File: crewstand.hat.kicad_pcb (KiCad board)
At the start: 2 copper layers, 113 x 70.5 mm, 21 parts, among them J2 CAN Terminal, J3 Sensor Terminal, J4 V-In, J5 Relais Out, J6 V-Out, Y1 12M

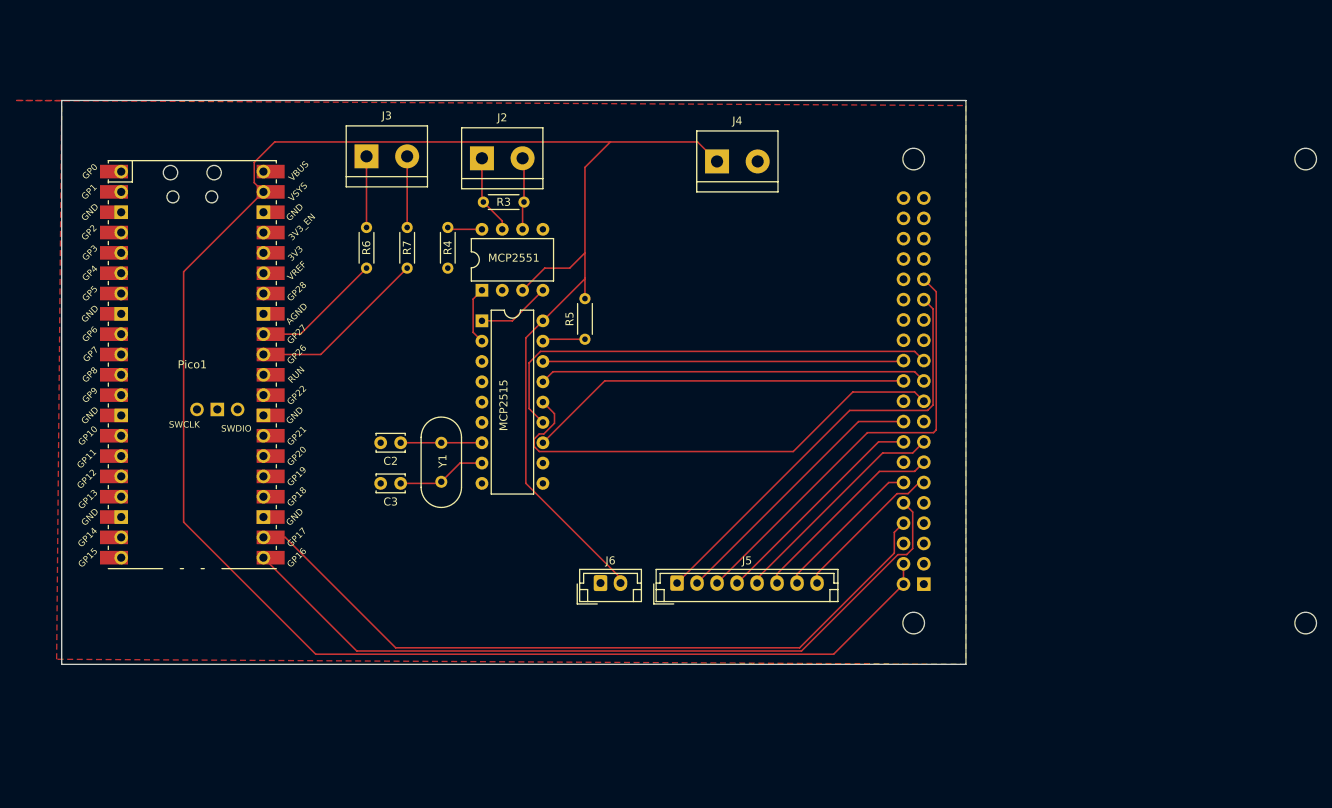
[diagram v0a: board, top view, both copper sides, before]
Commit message: feat: use jst connectors
* update clearance and track width
* Optimize placement and tracks

issue #2
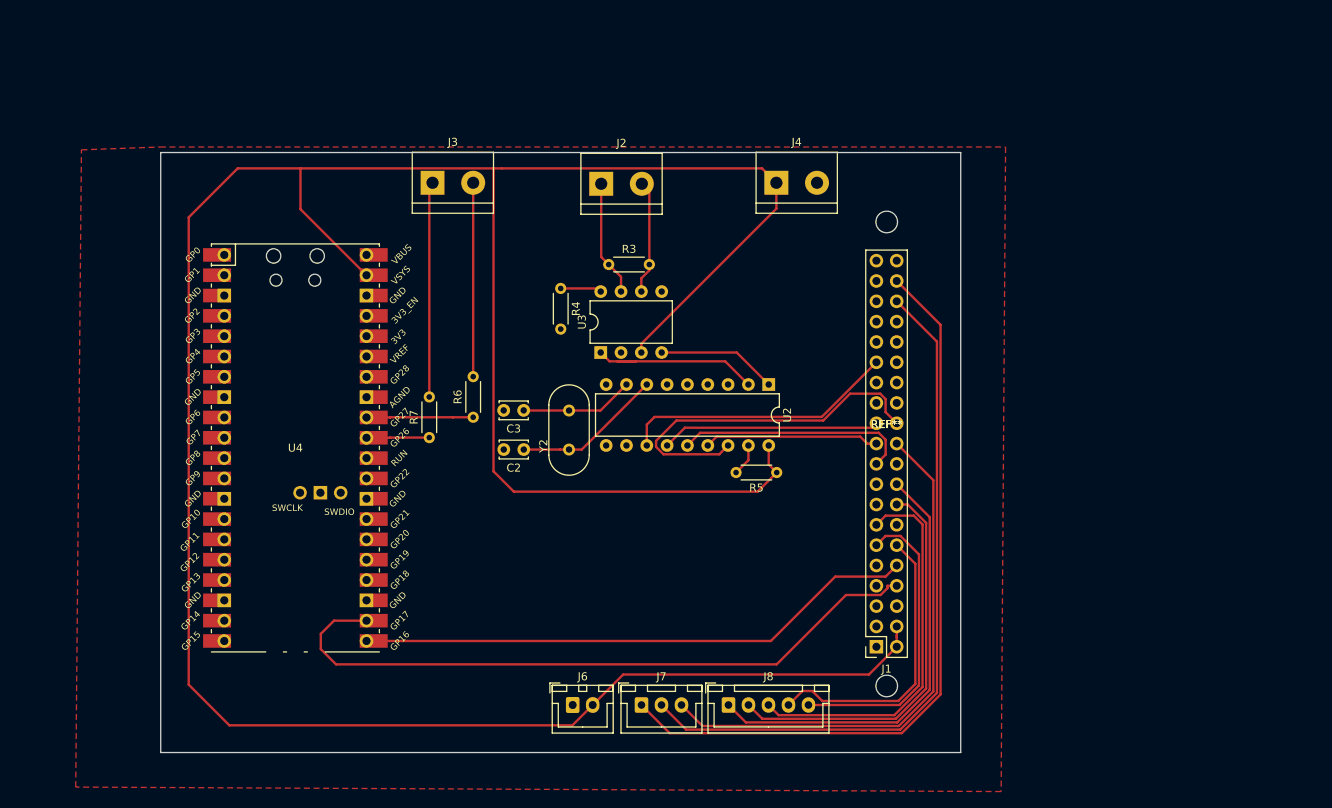
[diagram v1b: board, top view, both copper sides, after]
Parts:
- removed J5: Relais Out, Connector_JST:JST_EH_B8B-EH-A_1x08_P2.50mm_Vertical
- removed MCP2515: MCP2515-xSO, Package_DIP:DIP-18_W7.62mm
- removed MCP2551: MCP2551-I-P, Package_DIP:DIP-8_W7.62mm
- removed MH1, MH2, MH3, MH4: MountingHole_2.7mm_M2.5, MountingHole:MountingHole_2.7mm_M2.5
- removed Pico1: PicoW, RaspberryPi:RPi_PicoW_SMD_TH
- removed RPi1: GPIO, Connector_PinSocket_2.54mm:PinSocket_2x20_P2.54mm_Vertical
- removed Y1: 12M, Crystal:Crystal_HC49-U_Vertical
- added J1: GPIO, Connector_PinSocket_2.54mm:PinSocket_2x20_P2.54mm_Vertical, F.Cu at (249.5, 191.8)
- added J7: Relais2, Connector_JST:JST_XH_B3B-XH-A_1x03_P2.50mm_Vertical, F.Cu at (220.1, 199.1)
- added J8: Relais1, Connector_JST:JST_XH_B5B-XH-A_1x05_P2.50mm_Vertical, F.Cu at (231.0, 199.1)
- added REF** (x2): MountingHole_2.7mm_M2.5, MountingHole:MountingHole_2.7mm_M2.5, F.Cu at (250.8, 167.7)
- added U2: MCP2515-xSO, Package_DIP:DIP-18_W7.62mm, F.Cu at (236.0, 159.0)
- added U3: MCP2551-I-P, Package_DIP:DIP-8_W7.62mm, F.Cu at (215.0, 155.0)
- added U4: PicoW, RaspberryPI PicoW:RPi_PicoW_SMD_TH, F.Cu at (176.8, 166.9)
- added Y2: 12M, Crystal:Crystal_HC49-U_Vertical, F.Cu at (211.0, 167.1)
- J6: footprint Connector_JST:JST_EH_B2B-EH-A_1x02_P2.50mm_Vertical -> Connector_JST:JST_XH_B2B-XH-A_1x02_P2.50mm_Vertical
- moved R5 32.4 mm to (237.0, 170.0), turned to 180 degrees
- moved R6 22.9 mm to (199.1, 163.1)
- moved R7 21.4 mm to (193.6, 165.6)
- moved C3 17.9 mm to (205.4, 162.2)
- moved R3 17.5 mm to (216.0, 144.0)
- moved R4 16.0 mm to (210.0, 147.0)
- moved J6 15.6 mm to (211.5, 199.1)
- moved C2 15.4 mm to (205.4, 167.1)
- moved J2 15.2 mm to (215.1, 133.9)
- moved J3 8.89 mm to (194.0, 133.8)
- moved J4 7.88 mm to (237.0, 133.8)
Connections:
- R6 pad 2: Net-(J3-Pin_1) -> Net-(J3-Pin_2)
- R7 pad 2: Net-(J3-Pin_2) -> Net-(J3-Pin_1)
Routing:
- net /GPIO20/PCM.DIN: track 0.00 -> 94.8 mm
- net /GPIO16: track 0.00 -> 88.6 mm
- net +5V: track 289.5 -> 356.5 mm
- net /GPIO6: track 54.8 -> 0.00 mm
- net /GPIO11/SPI0.SCLK: track 58.6 -> 27.3 mm
- net /GPIO10/SPI0.MOSI: track 60.1 -> 29.3 mm
- net /GPIO22: track 28.5 -> 0.00 mm
- net /GPIO15/RXD0: track 97.5 -> 70.2 mm
- net /GPIO9/SPI0.MISO: track 48.6 -> 21.9 mm
- net /GPIO27: track 25.3 -> 48.3 mm
- net Net-(U2-RXCAN): track 0.00 -> 22.4 mm
- net /GPIO23: track 28.1 -> 49.8 mm
- net /GPIO24: track 34.2 -> 55.2 mm
- net /GPIO5: track 54.9 -> 34.5 mm
- net /GPIO25: track 48.3 -> 67.2 mm
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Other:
- board size 113 x 70.5 mm -> 100 x 75 mm

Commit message: feat: add mounting holes
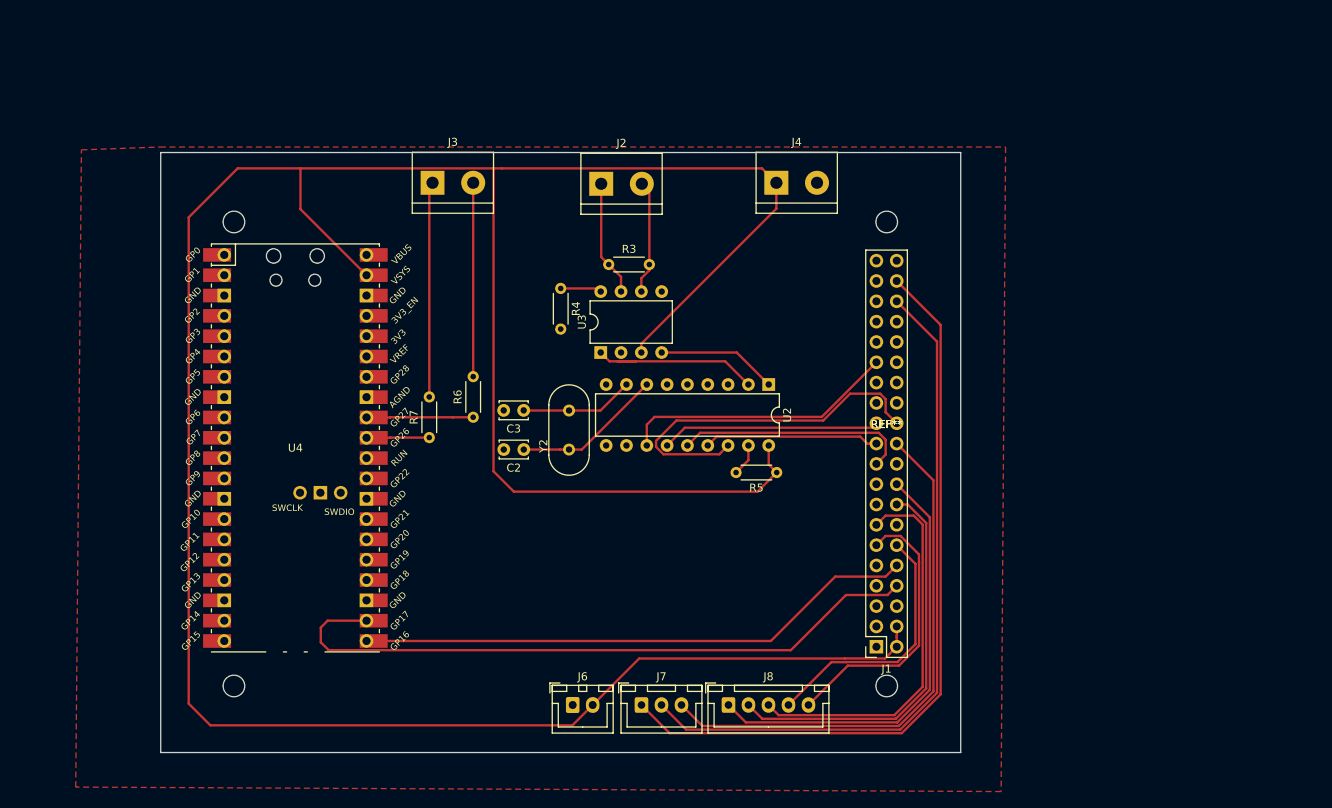
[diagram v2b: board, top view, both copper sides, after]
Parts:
- added ?: , , F.Cu at (169.2, 196.7)
- added ?: , , F.Cu at (169.2, 138.7)
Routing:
- net /GPIO18/PCM.CLK: track 36.3 -> 32.4 mm
- net /GPIO17: track 38.0 -> 35.1 mm
- net /GPIO14/TXD0: track 85.3 -> 83.6 mm
- net +5V: track 356.5 -> 357.8 mm

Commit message: feat: adopt voroni design
* do not use GND fill to optimize for voroni design
* voroni design for better milling
* milling paths generated with [pcb2gcode](https://github.com/pcb2gcode/pcb2gcode)
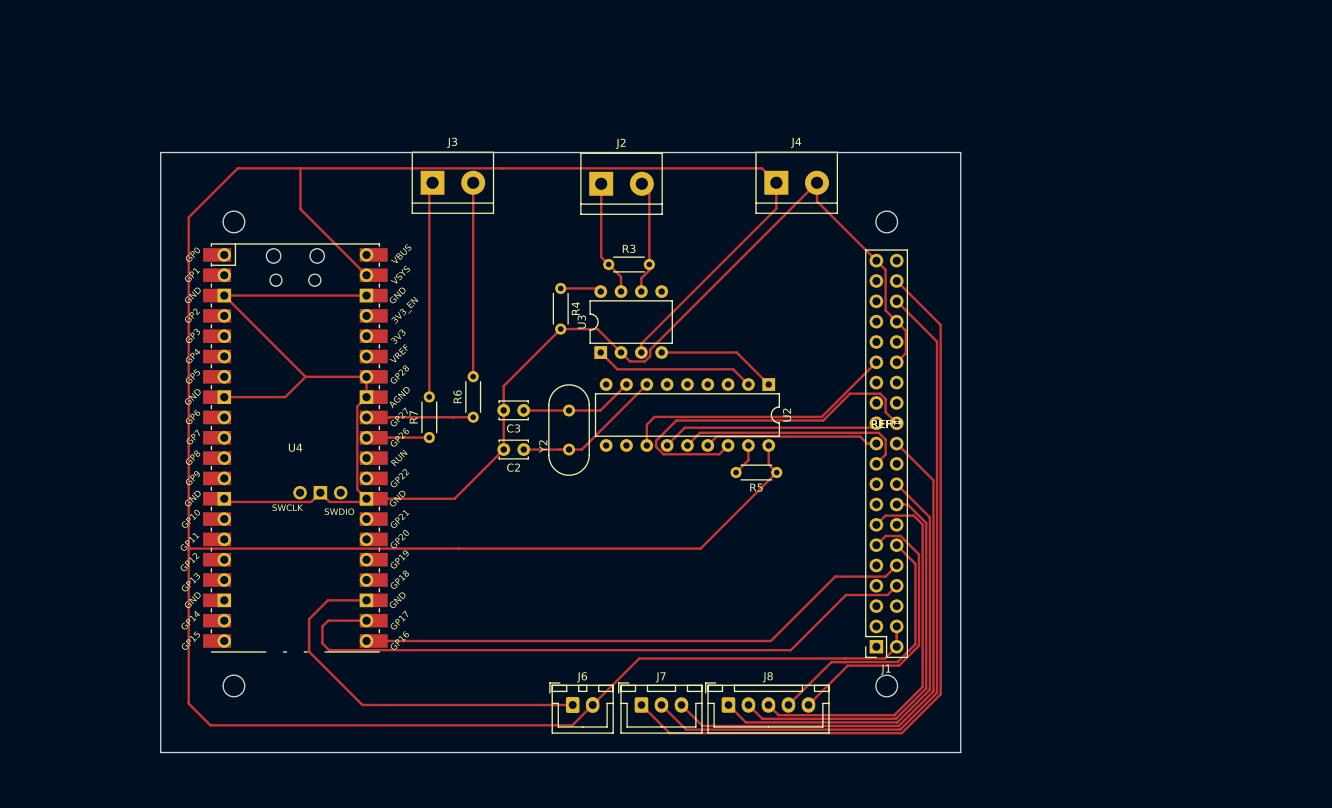
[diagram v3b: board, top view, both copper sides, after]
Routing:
- net GND: track 0.00 -> 242.8 mm
- net Net-(U2-RXCAN): track 22.4 -> 20.1 mm
- net +5V: track 357.8 -> 360.0 mm
- removed copper zone on F.Cu, net GND

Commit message: feat!: reorder for bottom placement
* Bottom placement needed to have connectors accessible on top
* optimize trace width
* optimise for voroni design
* include [pcb2gcode](https://github.com/pcb2gcode/pcb2gcode) generated svg for cnc

BREAKING CHANGE: Platine Layout for bottom
  placement of the Parts
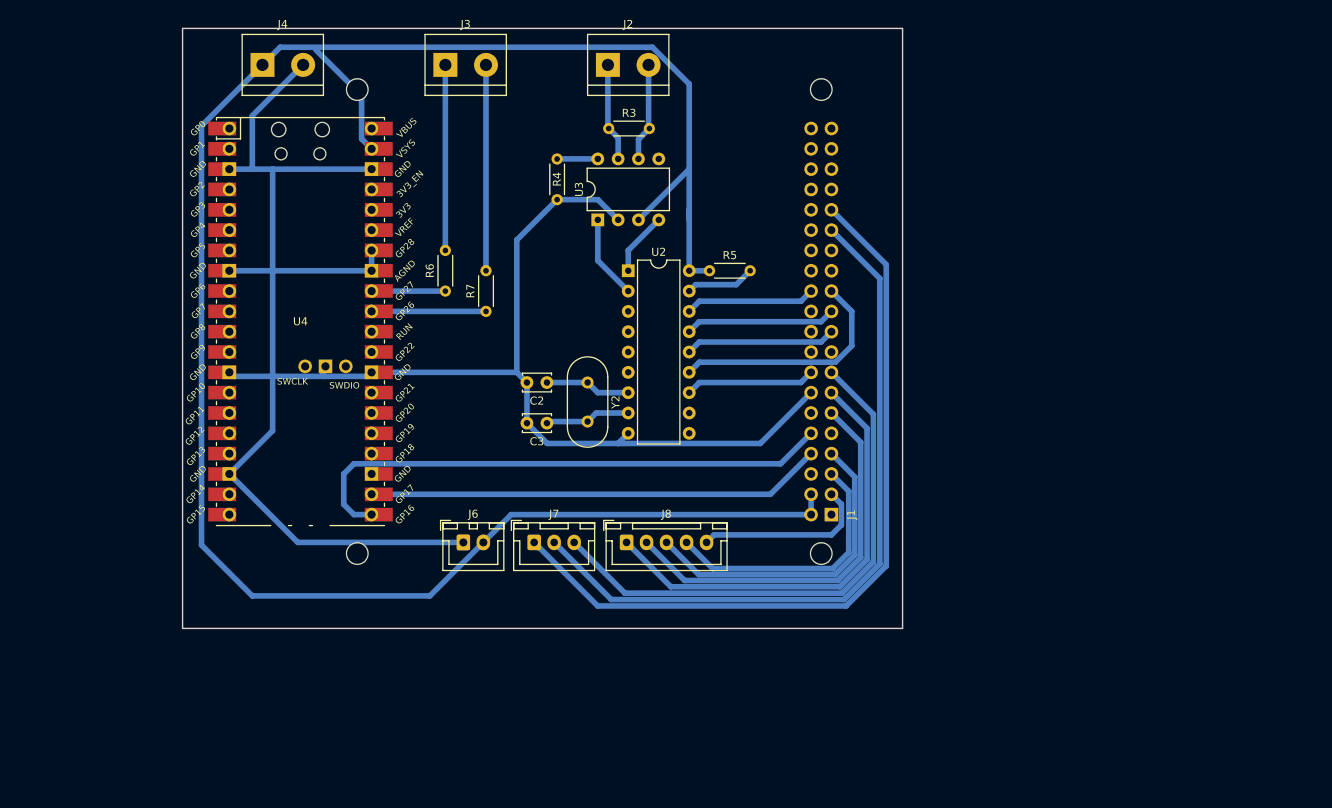
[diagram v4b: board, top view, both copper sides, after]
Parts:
- removed the ? at (169.2, 196.7)
- removed the ? at (169.2, 138.7)
- removed REF** (x2): MountingHole_2.7mm_M2.5, MountingHole:MountingHole_2.7mm_M2.5
- added ?: , , F.Cu at (184.6, 180.1)
- added ?: , , F.Cu at (184.6, 122.1)
- added MH1: MountingHole_2.7mm_M2.5, MountingHole:MountingHole_2.7mm_M2.5, F.Cu at (242.6, 180.1)
- added MH2: MountingHole_2.7mm_M2.5, MountingHole:MountingHole_2.7mm_M2.5, F.Cu at (242.6, 122.1)
- J1: moved to B.Cu
- moved J4 65.9 mm to (172.7, 119.0)
- moved R5 26.6 mm to (228.6, 144.8), turned to 0 degrees
- moved J6 24.5 mm to (197.8, 178.7)
- moved J7 24.3 mm to (206.7, 178.7)
- moved J8 24.0 mm to (218.2, 178.7)
- moved U2 22.6 mm to (218.4, 144.8), turned to 0 degrees
- moved J1 17.4 mm to (243.8, 175.3), turned to 0 degrees
- moved R7 17.3 mm to (200.7, 149.9)
- moved R3 17.0 mm to (216.0, 127.0)
- moved U3 16.6 mm to (214.6, 138.4)
- moved R4 16.2 mm to (209.6, 130.8)
- moved R6 16.2 mm to (195.6, 147.3)
- moved U4 15.8 mm to (177.5, 151.1)
- moved J2 14.9 mm to (215.9, 119.0)
- moved J3 14.8 mm to (195.6, 119.0)
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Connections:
- net /3.3 V renamed /3.3V
- J7 pad 1: /GPIO20/PCM.DIN -> /GPIO6
- J7 pad 2: /GPIO16 -> /GPIO5
- J7 pad 3: /GPIO25 -> /GPIO22
- J8 pad 1: /GPIO24 -> /GPIO27
- J8 pad 2: /GPIO23 -> /GPIO17
- J8 pad 3: /GPIO27 -> /GPIO4/GPCLK0
- J8 pad 4: /GPIO18/PCM.CLK -> /GPIO3/SCL1
- J8 pad 5: /GPIO17 -> /GPIO2/SDA1
- R6 pad 2: Net-(J3-Pin_2) -> Net-(J3-Pin_1)
- R7 pad 2: Net-(J3-Pin_1) -> Net-(J3-Pin_2)
- U2 pad 12: /GPIO5 -> /GPIO23
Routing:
- net +5V: track 360.0 -> 256.3 mm
- net /GPIO6: track 0.00 -> 96.7 mm
- net /GPIO20/PCM.DIN: track 94.8 -> 0.00 mm
- net /GPIO16: track 88.6 -> 0.00 mm
- net /GPIO22: track 0.00 -> 67.5 mm
- net /GPIO25: track 67.3 -> 0.00 mm
- net /GPIO5: track 34.5 -> 89.7 mm
- net /GPIO24: track 55.2 -> 0.00 mm
- net /GPIO4/GPCLK0: track 0.00 -> 40.1 mm
- net /GPIO23: track 49.8 -> 16.3 mm
- net /GPIO3/SCL1: track 0.00 -> 33.2 mm
- net /GPIO18/PCM.CLK: track 32.4 -> 0.00 mm
- net /GPIO8/SPI0.CE0: track 45.6 -> 16.3 mm
- net /GPIO14/TXD0: track 83.4 -> 57.0 mm
- net /GPIO2/SDA1: track 0.00 -> 22.1 mm
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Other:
- board size 100 x 75 mm -> 90 x 75 mm

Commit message: fix(Sensors): correct resistor placement for analog sensor readings
- Move pull-down resistors from sensor-to-ADC path to ADC-to-GND
- Update schematic to implement proper current-to-voltage conversion

Breaking Change: Yes
- PCB layout updated
- Existing boards will need rework to implement this fix

Resolves: #6
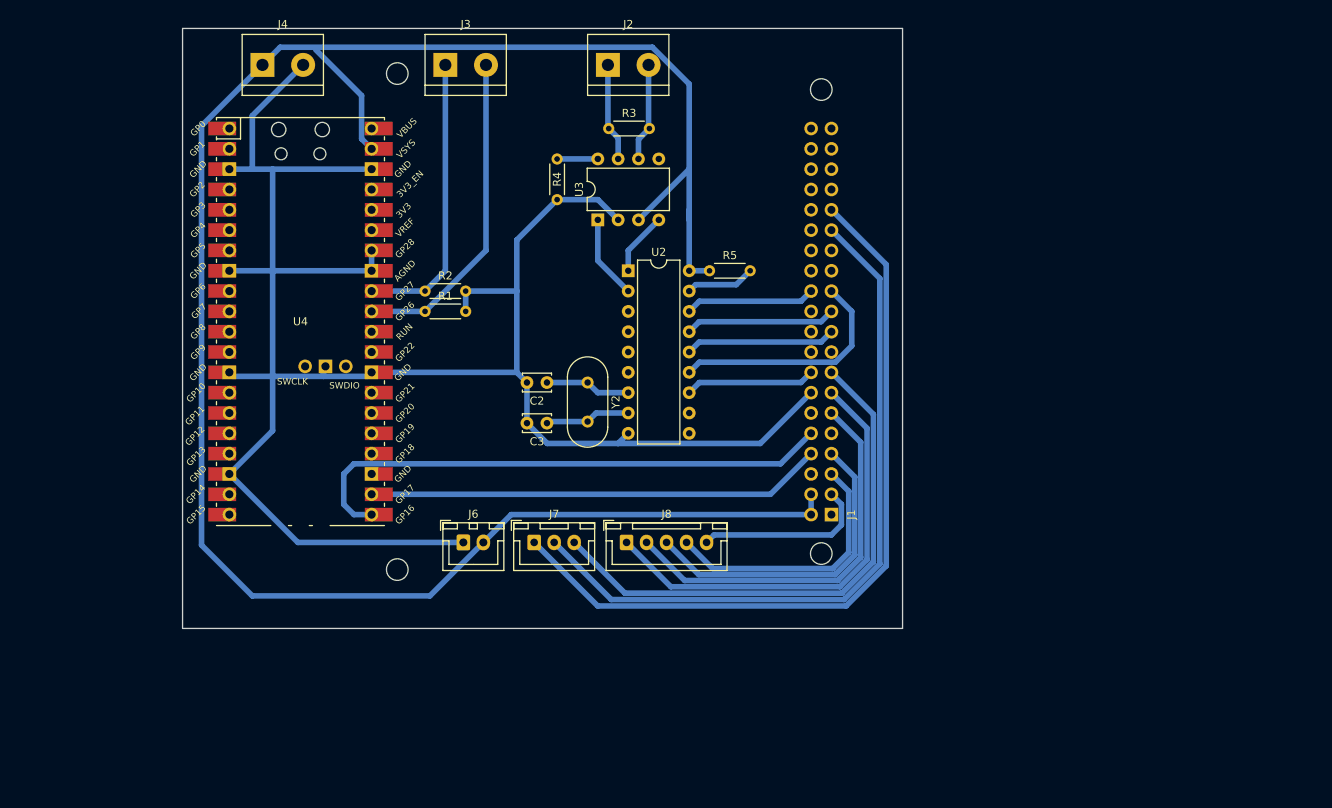
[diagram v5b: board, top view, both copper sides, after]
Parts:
- removed R6, R7: 300, Resistor_THT:R_Axial_DIN0204_L3.6mm_D1.6mm_P5.08mm_Horizontal
- added R1: 300, Resistor_THT:R_Axial_DIN0204_L3.6mm_D1.6mm_P5.08mm_Horizontal, F.Cu at (193.0, 149.9)
- added R2: 300, Resistor_THT:R_Axial_DIN0204_L3.6mm_D1.6mm_P5.08mm_Horizontal, F.Cu at (193.0, 147.3)
- moved ? 5.39 mm to (189.6, 182.1)
- moved ? 5.39 mm to (189.6, 120.1)
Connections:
- U4 pad 31: /ADC0 -> Net-(J3-Pin_2)
- U4 pad 32: /ADC1 -> Net-(J3-Pin_1)
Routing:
- net Net-(J3-Pin_2): track 25.7 -> 40.6 mm
- net /ADC0: track 14.3 -> 0.00 mm
- net Net-(J3-Pin_1): track 23.2 -> 36.0 mm
- net /ADC1: track 9.22 -> 0.00 mm
- net GND: track 244.8 -> 253.8 mm
